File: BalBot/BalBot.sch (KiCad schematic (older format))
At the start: 41 parts, among them P1 FTSH-105-01-F-DV, P2 USB_OTG, P3 CONN_01X11, P4 CONN_01X11, Q1 DTC114E, SW1 SW_RST, SW2 SW_USR1, SW3 SW_USR2, U1 TM4C123GH6PM, U2 ESP01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

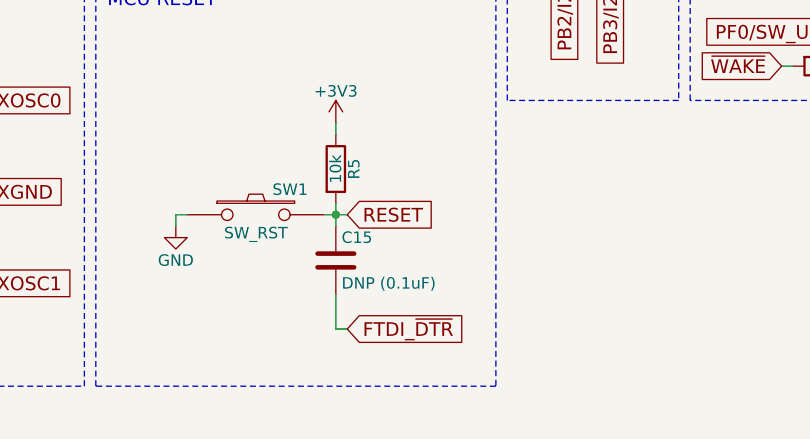
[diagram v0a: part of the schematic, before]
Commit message: Started layout
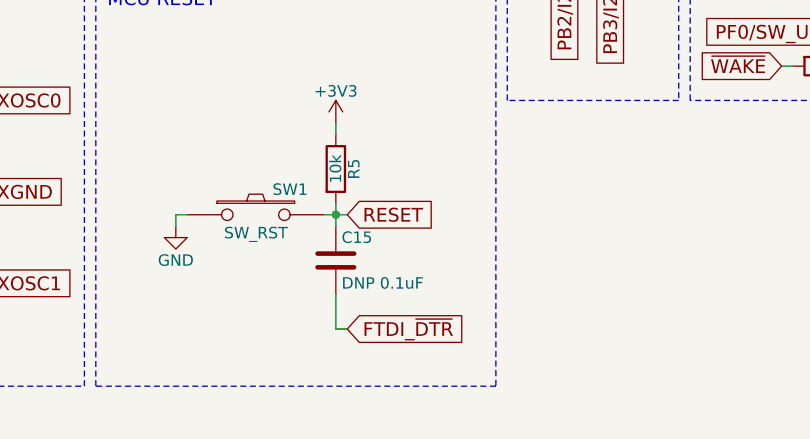
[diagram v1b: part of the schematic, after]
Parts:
- C12: footprint (none) -> Capacitors_SMD:C_0603; Digikey (none) -> 490-3296-1-ND
- C15: value DNP (0.1uF) -> DNP 0.1uF; footprint (none) -> Capacitors_SMD:C_0402; DigiKey (none) -> 490-9997-1-ND
- D1, D2: footprint (none) -> LEDs:LED_0805
- JP1: footprint (none) -> _BalBotLib:Jumper_NC
- P1: footprint (none) -> Pin_Headers:Pin_Header_Straight_2x05_Pitch1.00mm_SMD
- P2: footprint (none) -> Connect:USB_Micro-B; DigiKey (none) -> 609-4613-1-ND
- P3, P4: footprint (none) -> Pin_Headers:Pin_Header_Straight_1x11_Pitch2.54mm
- Q1: footprint (none) -> _BalBotLib:SOT-416; DigiKey (none) -> DTC114EET1GOSCT-ND
- R1, R10, R9: footprint (none) -> Resistors_SMD:R_0805; DigiKey (none) -> 311-100CRCT-ND
- R2, R3, R4, R5: footprint (none) -> Resistors_SMD:R_0805; DigiKey (none) -> 311-10.0KCRCT-ND
- R6, R7: footprint (none) -> Resistors_SMD:R_0805; DigiKey (none) -> 311-4.70KCRCT-ND
- R8: footprint (none) -> Resistors_SMD:R_0805; DigiKey (none) -> 311-330CRCT-ND
- SW1, SW2, SW3: footprint (none) -> _BalBotLib:SW_SPST_6x6mm; DigiKey (none) -> CKN9112CT-ND
- U1: footprint (none) -> Housings_QFP:LQFP-64_10x10mm_Pitch0.5mm
- U2: footprint (none) -> Pin_Headers:Pin_Header_Straight_2x04_Pitch2.54mm
- U3: footprint (none) -> Pin_Headers:Pin_Header_Straight_1x06_Pitch2.54mm
- Y1: footprint (none) -> Crystals:Crystal_SMD_5032-2pin_5.0x3.2mm; DigiKey (none) -> 644-1037-1-ND
- Y2: footprint (none) -> _BalBotLib:Crystal_32768Hz_Radial_Can; DigiKey (none) -> 535-9033-1-ND

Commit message: Working On Layout
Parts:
- P2: symbol USB_OTG -> USB_OTG-RESCUE-BalBot; DigiKey 609-4613-1-ND -> 609-4618-1-ND
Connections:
- net XOSC0: now also C14.2, Y2.1; no longer C13.1, Y2.2
- net XOSC1: now also C13.1, Y2.2; no longer C14.2, Y2.1
- net PD4/USB0_DM renamed USB0_D-
- net PD5/USB0_DP renamed USB0_D+
